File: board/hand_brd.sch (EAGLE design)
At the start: 133 parts, among them IC1 FT230XS, Q1 BC847ALT1SMD, Q2 16MHz, Q3 16MHz, U2 ATXMEGA128D4-AU

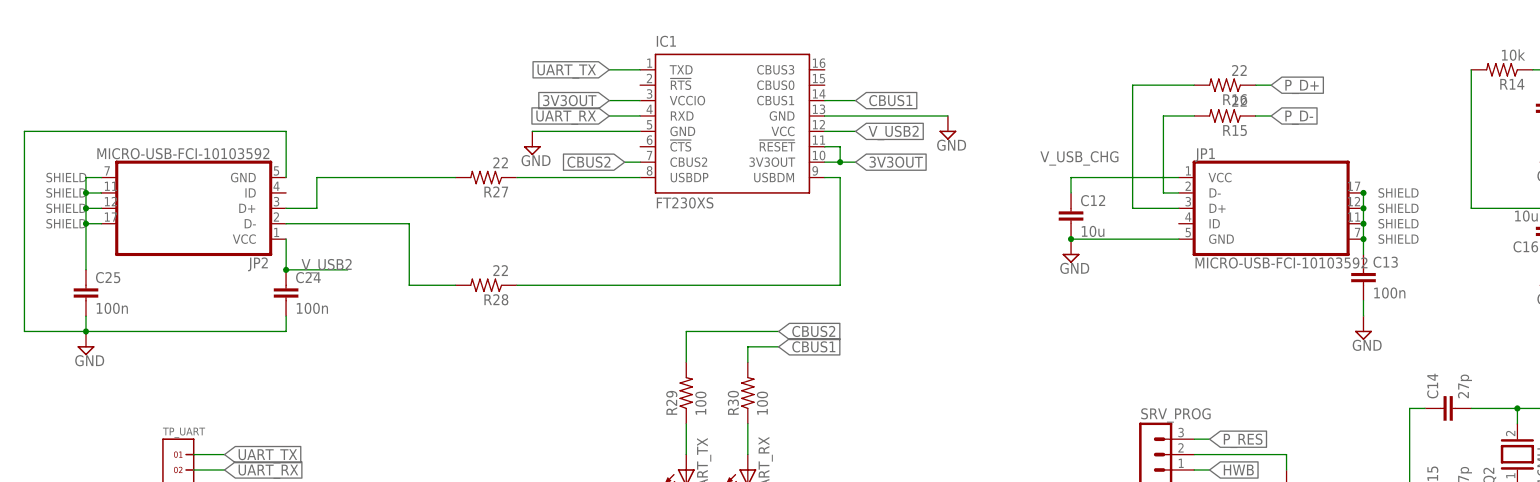
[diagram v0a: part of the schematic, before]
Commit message: Fix wrong USB model
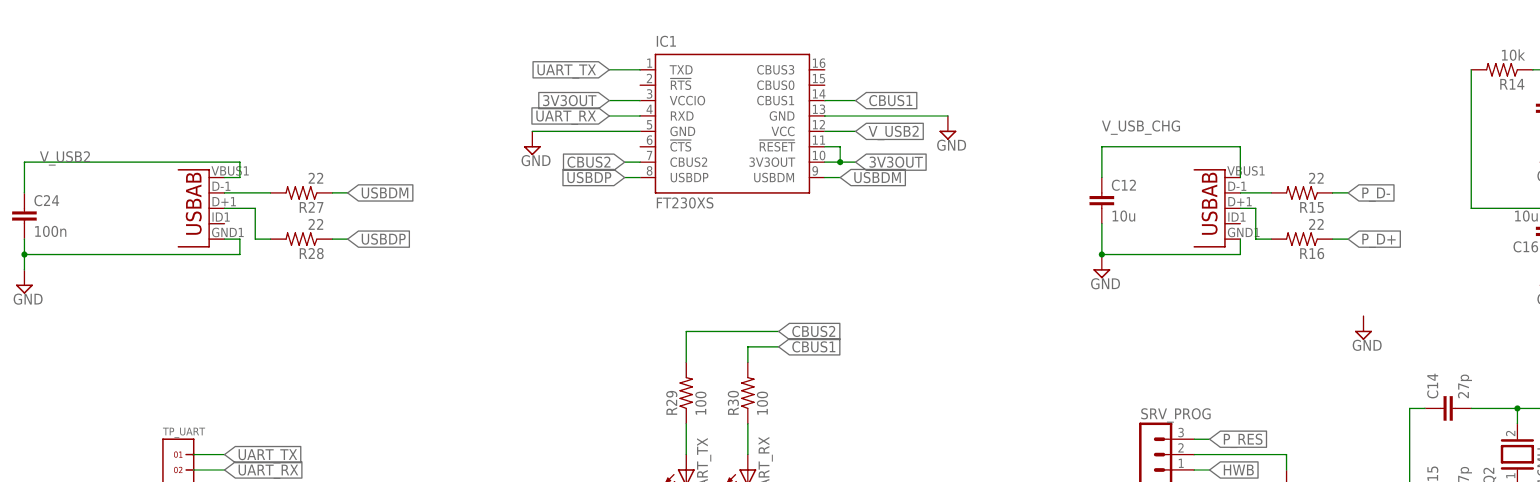
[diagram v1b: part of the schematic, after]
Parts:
- removed C13, C25: 100n, rcl:C-EUC0805K
- removed JP1, JP2: MICRO-USB-FCI-10103592, micro-usb-fci-10103592:MICRO-USB-FCI-10103592
- added U1, U3: (no value), MicroUSB:USB""
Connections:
- removed net N$11: JP1.D+, R16.2
- removed net N$23: IC1.USBDM, R28.1
- removed net USB2_D+: JP2.D+, R27.2
- removed net USB2_D-: JP2.D-, R28.2
- new net USBDM: IC1.USBDM, R27.1
- new net USBDP: IC1.USBDP, R28.1
- net GND: now also U1.GND, U3.GND; no longer C13.2, C25.2, JP1.GND, JP2.GND
- net N$10: now also U3.D-; no longer JP1.D-
- net N$18: now also R27.2, U1.D-; no longer C25.1
- net N$22: now also R28.2, U1.D+; no longer IC1.USBDP, R27.1
- net N$8: now also R16.2, U3.D+; no longer C13.1
- net V_USB2: now also U1.VBUS; no longer JP2.VCC
- net V_USB_CHG: now also U3.VBUS; no longer JP1.VCC
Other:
- moved on the sheet: C12, C24, R15, R16, R27, R28

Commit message: Add missing diode
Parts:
- added U$26: PMEG2010ET, pol:PMEG2010ET
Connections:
- new net N$11: R20.2, U$26.C
- net N$14: now also U$26.A; no longer R20.2
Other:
- moved on the sheet: R20
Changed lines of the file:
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@@
 <part name="U1" library="MicroUSB" deviceset="USB" device="&quot;&quot;"/>
 <part name="U3" library="MicroUSB" deviceset="USB" device="&quot;&quot;"/>
+<part name="U$26" library="pol" deviceset="PMEG2010ET" device=""/>
 </parts>
 <sheets>
@@
 <instance part="R18" gate="G$1" x="-45.72" y="111.76" rot="R180"/>
 <instance part="R19" gate="G$1" x="-45.72" y="119.38" rot="R180"/>
-<instance part="R20" gate="G$1" x="-45.72" y="127" rot="R180"/>
+<instance part="R20" gate="G$1" x="-40.64" y="127" rot="R180"/>
 <instance part="R21" gate="G$1" x="-45.72" y="139.7"/>
 <instance part="R13" gate="G$1" x="-45.72" y="177.8" rot="R180"/>
@@
 <instance part="U1" gate="G$1" x="-370.84" y="149.86" rot="R180"/>
 <instance part="U3" gate="G$1" x="-203.2" y="149.86" rot="R180"/>
+<instance part="U$26" gate="G$1" x="-50.8" y="127"/>
 </instances>
 <busses>
@@
 <pinref part="U$13" gate="AT90USB162" pin="(XCK/PCINT12)PD5"/>
 <wire x1="-71.12" y1="119.38" x2="-58.42" y2="119.38" width="0.1524" layer="91"/>
-<wire x1="-58.42" y1="119.38" x2="-58.42" y2="127" width="0.1524" layer="91"/>
-<pinref part="R20" gate="G$1" pin="2"/>
-<wire x1="-58.42" y1="127" x2="-50.8" y2="127" width="0.1524" layer="91"/>
+<pinref part="U$26" gate="G$1" pin="A"/>
+<wire x1="-53.34" y1="127" x2="-58.42" y2="127" width="0.1524" layer="91"/>
+<wire x1="-58.42" y1="127" x2="-58.42" y2="119.38" width="0.1524" layer="91"/>
 </segment>
 </net>
@@
 <segment>
 <pinref part="R20" gate="G$1" pin="1"/>
-<wire x1="-40.64" y1="127" x2="-30.48" y2="127" width="0.1524" layer="91"/>
+<wire x1="-35.56" y1="127" x2="-30.48" y2="127" width="0.1524" layer="91"/>
 <label x="-30.48" y="127" size="1.778" layer="95" xref="yes"/>
 </segment>
@@
 </segment>
 </net>
+<net name="N$11" class="0">
+<segment>
+<pinref part="R20" gate="G$1" pin="2"/>
+<pinref part="U$26" gate="G$1" pin="C"/>
+<wire x1="-45.72" y1="127" x2="-48.26" y2="127" width="0.1524" layer="91"/>
+</segment>
+</net>

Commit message: Remove unused connection for disabling the boost converters and shuffle things around a bit to have a better ground plane
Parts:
- removed U$11, U$12: PMEG2010ET, pol:PMEG2010ET
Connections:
- removed net N$6: R12.2, U$11.C, U$12.C
- net BATT_LOW: now also R12.2; no longer U$11.A
- net V_USB_CHG: no longer U$12.A
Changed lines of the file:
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@@
 <part name="Q1" library="transistor-npn" deviceset="BC847*" device="SMD" technology="ALT1"/>
 <part name="SUPPLY11" library="supply2" deviceset="GND" device=""/>
-<part name="U$11" library="pol" deviceset="PMEG2010ET" device=""/>
-<part name="U$12" library="pol" deviceset="PMEG2010ET" device=""/>
 <part name="R11" library="rcl" deviceset="R-US_" device="M0805" value="10k"/>
 <part name="R12" library="rcl" deviceset="R-US_" device="M0805" value="10k"/>
@@
 <instance part="Q1" gate="G$1" x="-81.28" y="63.5"/>
 <instance part="SUPPLY11" gate="GND" x="-78.74" y="55.88"/>
-<instance part="U$11" gate="G$1" x="-104.14" y="58.42"/>
-<instance part="U$12" gate="G$1" x="-104.14" y="68.58"/>
 <instance part="R11" gate="G$1" x="-78.74" y="78.74" rot="R90"/>
 <instance part="R12" gate="G$1" x="-91.44" y="63.5" rot="R180"/>
@@
 </segment>
 </net>
-<net name="N$6" class="0">
-<segment>
-<pinref part="U$12" gate="G$1" pin="C"/>
-<wire x1="-101.6" y1="68.58" x2="-99.06" y2="68.58" width="0.1524" layer="91"/>
-<wire x1="-99.06" y1="68.58" x2="-99.06" y2="63.5" width="0.1524" layer="91"/>
-<pinref part="U$11" gate="G$1" pin="C"/>
-<wire x1="-99.06" y1="63.5" x2="-99.06" y2="58.42" width="0.1524" layer="91"/>
-<wire x1="-99.06" y1="58.42" x2="-101.6" y2="58.42" width="0.1524" layer="91"/>
-<pinref part="R12" gate="G$1" pin="2"/>
-<wire x1="-99.06" y1="63.5" x2="-96.52" y2="63.5" width="0.1524" layer="91"/>
-<junction x="-99.06" y="63.5"/>
-</segment>
-</net>
 <net name="V_USB_CHG" class="0">
-<segment>
-<pinref part="U$12" gate="G$1" pin="A"/>
-<wire x1="-106.68" y1="68.58" x2="-111.76" y2="68.58" width="0.1524" layer="91"/>
-<label x="-111.76" y="68.58" size="1.778" layer="95" rot="R180" xref="yes"/>
-</segment>
 <segment>
 <pinref part="C12" gate="G$1" pin="1"/>
@@
 <net name="BATT_LOW" class="0">
 <segment>
-<pinref part="U$11" gate="G$1" pin="A"/>
-<wire x1="-106.68" y1="58.42" x2="-111.76" y2="58.42" width="0.1524" layer="91"/>
-<label x="-111.76" y="58.42" size="1.778" layer="95" rot="R180" xref="yes"/>
-</segment>
-<segment>
 <pinref part="U2" gate="G$1" pin="PC7"/>
 <wire x1="-99.06" y1="-22.86" x2="-96.52" y2="-22.86" width="0.1524" layer="91"/>
 <label x="-96.52" y="-22.86" size="1.778" layer="95" xref="yes"/>
 </segment>
-</net>
+<segment>
+<pinref part="R12" gate="G$1" pin="2"/>
+<wire x1="-96.52" y1="63.5" x2="-104.14" y2="63.5" width="0.1524" layer="91"/>
+<label x="-104.14" y="63.5" size="1.778" layer="95" rot="R180" xref="yes"/>
+</segment>
+</net>
